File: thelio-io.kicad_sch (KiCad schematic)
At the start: 23 parts, among them Y1 16MHz

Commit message: Layout improvements
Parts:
- USB1: footprint Connector_PinHeader_2.54mm:PinHeader_1x04_P2.54mm_Vertical -> USB:USB_IDC
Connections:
- net GND: now also USB1.7 (GND); no longer USB1.4 (GND)
- net at R1.1: now also USB1.5 (D+); no longer USB1.3 (D+)
- net at USB1.2 (VBUS): no longer R2.1
- new net: R2.1, USB1.3 (D-)
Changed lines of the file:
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@@
       (effects (font (size 1.27 1.27)) hide)
     )
-    (property "Datasheet" "http://www.ti.com/lit/ds/symlink/sn74lvc2g157.pdf" (id 3) (at 200.66 33.02 0)
+    (property "Datasheet" "http://www.ti.com/lit/sg/scyt129e/scyt129e.pdf" (id 3) (at 200.66 33.02 0)
       (effects (font (size 1.27 1.27)) hide)
     )
@@
       (effects (font (size 1.27 1.27)) hide)
     )
-    (property "Datasheet" "" (id 3) (at 183.515 113.03 0)
+    (property "Datasheet" "~" (id 3) (at 183.515 113.03 0)
       (effects (font (size 1.27 1.27)) hide)
     )
@@
       (effects (font (size 1.27 1.27)) hide)
     )
-    (property "Datasheet" "" (id 3) (at 229.235 113.03 0)
+    (property "Datasheet" "~" (id 3) (at 229.235 113.03 0)
       (effects (font (size 1.27 1.27)) hide)
     )
@@
       (effects (font (size 1.27 1.27)) hide)
     )
-    (property "Datasheet" "http://www.ti.com/lit/ds/symlink/sn74lvc2g157.pdf" (id 3) (at 229.87 33.02 0)
+    (property "Datasheet" "http://www.ti.com/lit/sg/scyt129e/scyt129e.pdf" (id 3) (at 229.87 33.02 0)
       (effects (font (size 1.27 1.27)) hide)
     )
@@
   (symbol (lib_id "USB:USB_IDC") (at 111.76 73.66 270) (mirror x) (unit 1)
     (in_bom yes) (on_board yes)
-    (property "Reference" "USB1" (id 0) (at 119.0752 72.6186 90)
-      (effects (font (size 1.27 1.27)) (justify left))
-    )
-    (property "Value" "USB_IDC" (id 1) (at 119.0752 74.93 90)
-      (effects (font (size 1.27 1.27)) (justify left))
-    )
-    (property "Footprint" "Connector_PinHeader_2.54mm:PinHeader_1x04_P2.54mm_Vertical" (id 2) (at 111.76 73.66 0)
+    (property "Reference" "USB1" (id 0) (at 110.49 56.515 90)
+      (effects (font (size 1.27 1.27)) (justify left))
+    )
+    (property "Value" "USB_IDC" (id 1) (at 110.49 66.3448 90)
+      (effects (font (size 1.27 1.27)) (justify left))
+    )
+    (property "Footprint" "USB:USB_IDC" (id 2) (at 111.76 73.66 0)
       (effects (font (size 1.27 1.27)) hide)
     )
@@
     (pin "3")
     (pin "4")
+    (pin "5")
+    (pin "6")
+    (pin "7")
+    (pin "8")
   )
   (symbol (lib_id "power:+12V") (at 266.065 54.61 270) (unit 1)
@@
       (effects (font (size 1.27 1.27)) hide)
     )
-    (property "Datasheet" "http://www.ti.com/lit/ds/symlink/sn74lvc2g157.pdf" (id 3) (at 172.085 33.02 0)
+    (property "Datasheet" "http://www.ti.com/lit/sg/scyt129e/scyt129e.pdf" (id 3) (at 172.085 33.02 0)
       (effects (font (size 1.27 1.27)) hide)
     )
@@
       (effects (font (size 1.27 1.27)) hide)
     )
-    (property "Datasheet" "" (id 3) (at 210.82 86.36 0)
+    (property "Datasheet" "~" (id 3) (at 210.82 86.36 0)
       (effects (font (size 1.27 1.27)) hide)
     )
@@
       (effects (font (size 1.27 1.27)) hide)
     )
-    (property "Datasheet" "http://www.ti.com/lit/ds/symlink/sn74lvc2g157.pdf" (id 3) (at 258.445 33.02 0)
+    (property "Datasheet" "http://www.ti.com/lit/sg/scyt129e/scyt129e.pdf" (id 3) (at 258.445 33.02 0)
       (effects (font (size 1.27 1.27)) hide)
     )
@@
     )
     (path "/24da91e1-4b2d-4e79-a096-b2424715c2dc"
-      (reference "USB1") (unit 1) (value "USB_IDC") (footprint "Connector_PinHeader_2.54mm:PinHeader_1x04_P2.54mm_Vertical")
+      (reference "USB1") (unit 1) (value "USB_IDC") (footprint "USB:USB_IDC")
     )
     (path "/ee06c0cd-13b9-4549-a21e-0082e6f6e36d"

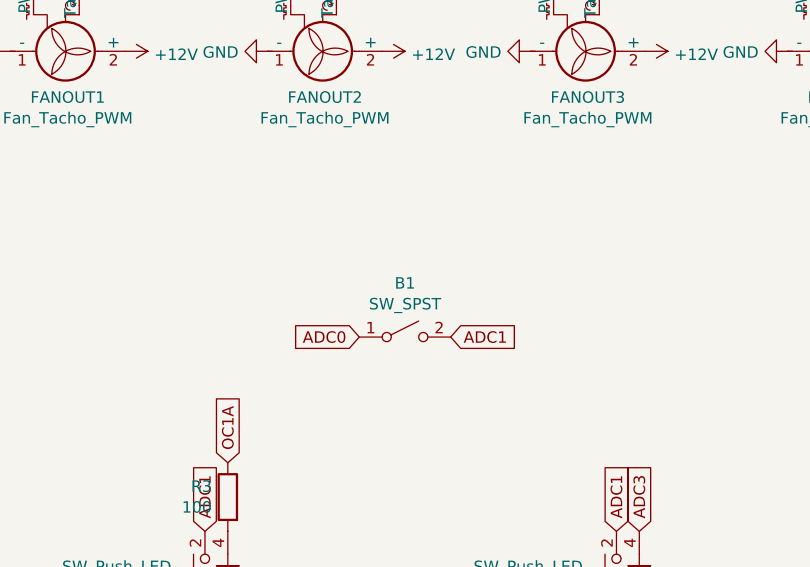
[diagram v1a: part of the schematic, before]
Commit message: Add logo and fix keepouts
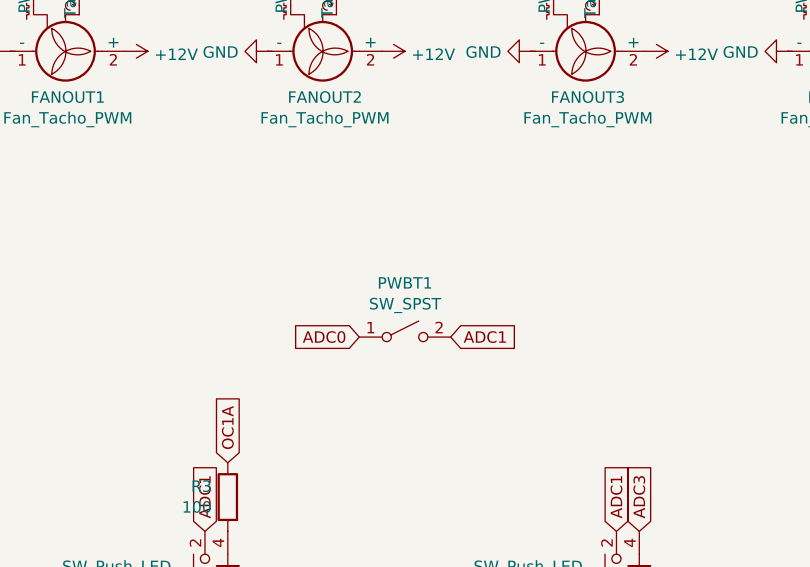
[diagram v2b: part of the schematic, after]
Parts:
- renumbered B1 to PWBT1
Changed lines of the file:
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@@
   (symbol (lib_id "Switch:SW_SPST") (at 210.82 86.36 0) (unit 1)
     (in_bom yes) (on_board yes)
-    (property "Reference" "B1" (id 0) (at 210.82 80.391 0))
+    (property "Reference" "PWBT1" (id 0) (at 210.82 80.391 0))
     (property "Value" "SW_SPST" (id 1) (at 210.82 82.7024 0))
     (property "Footprint" "Button_Switch_SMD:SW_SPST_TL3342" (id 2) (at 210.82 86.36 0)
@@
       (reference "AVR1") (unit 1) (value "ATmega32U4-AU") (footprint "Package_DFN_QFN:QFN-64-1EP_9x9mm_P0.5mm_EP7.5x7.5mm")
     )
-    (path "/7e939f07-8642-4689-8727-9660b52fff9f"
-      (reference "B1") (unit 1) (value "SW_SPST") (footprint "Button_Switch_SMD:SW_SPST_TL3342")
-    )
     (path "/95d7b4e4-d090-4b4b-95d7-0687255342ed"
       (reference "C1") (unit 1) (value "22pF") (footprint "Capacitor_SMD:C_0402_1005Metric")
@@
       (reference "POWER1") (unit 1) (value "ATA_FLOPPY_POWER_4") (footprint "SATA:ATA_FLOPPY_POWER_4")
     )
+    (path "/7e939f07-8642-4689-8727-9660b52fff9f"
+      (reference "PWBT1") (unit 1) (value "SW_SPST") (footprint "Button_Switch_SMD:SW_SPST_TL3342")
+    )
     (path "/0a7c8d68-eedc-46bd-8a41-9ec0add1f19c"

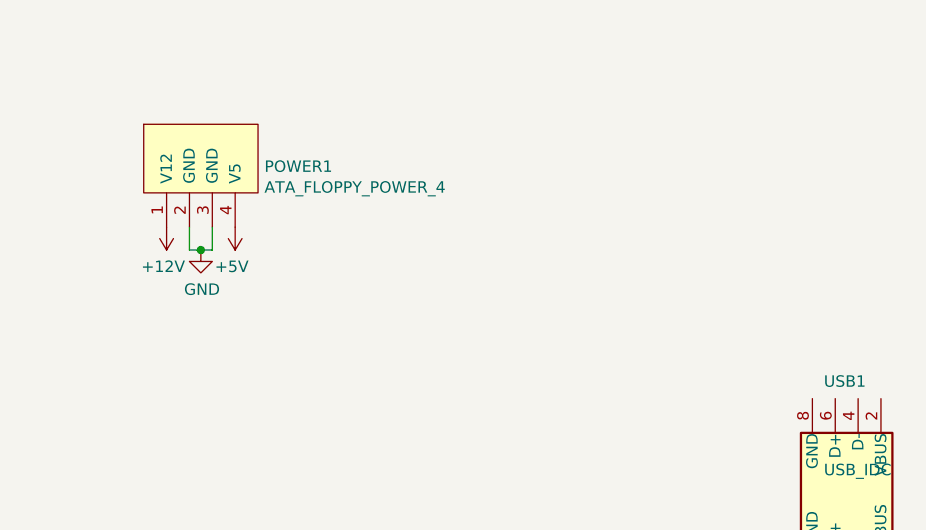
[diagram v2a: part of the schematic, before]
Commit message: Make 4-layer and improve fills
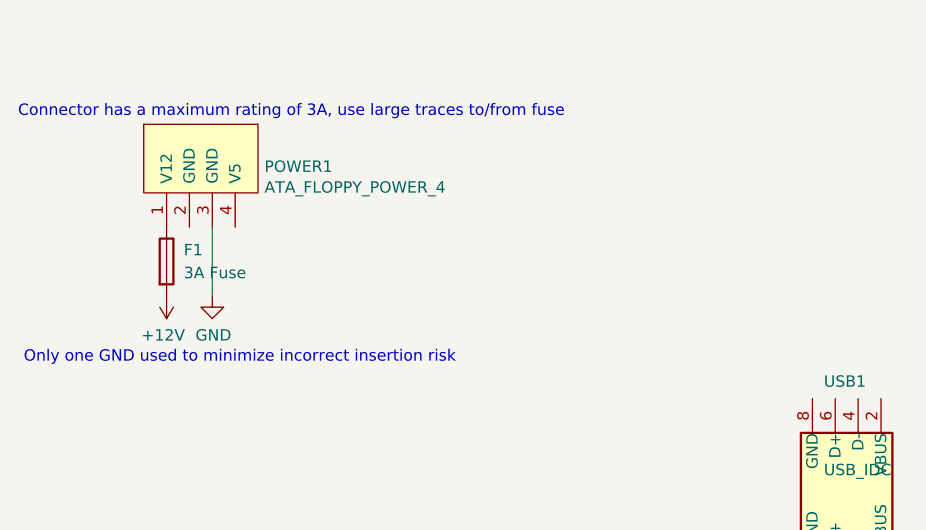
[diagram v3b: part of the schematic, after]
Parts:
- added F1: 3A Fuse, Fuse:Fuse_0603_1608Metric, symbol Device:Fuse
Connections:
- net +12V: now also F1.2; no longer POWER1.1 (V12)
- net GND: no longer POWER1.2 (GND)
- net +5V: no longer names the net of POWER1.4 (V5)
- new net: F1.1, POWER1.1 (V12)
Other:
- note added: "Connector has a maximum rating of 3A, use large traces to/from fuse"
- note added: "Only one GND used to minimize incorrect insertion risk"
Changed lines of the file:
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@@
 (kicad_sch (version 20211123) (generator eeschema)
   (paper "A4")
-  (junction (at 41.275 41.91) (diameter 0) (color 0 0 0 0)
-  )
   (junction (at 133.35 96.52) (diameter 0) (color 0 0 0 0)
   )
@@
   (junction (at 125.73 96.52) (diameter 0) (color 0 0 0 0)
   )
-  (wire (pts (xy 40.005 41.91) (xy 41.275 41.91))
-    (stroke (width 0) (type default) (color 0 0 0 0))
-  )
   (wire (pts (xy 104.14 104.14) (xy 104.14 101.6))
     (stroke (width 0) (type default) (color 0 0 0 0))
@@
     (stroke (width 0) (type default) (color 0 0 0 0))
   )
+  (wire (pts (xy 42.545 39.37) (xy 42.545 46.99))
+    (stroke (width 0) (type default) (color 0 0 0 0))
+  )
   (wire (pts (xy 111.76 92.71) (xy 111.76 104.14))
     (stroke (width 0) (type default) (color 0 0 0 0))
   )
-  (wire (pts (xy 42.545 39.37) (xy 42.545 41.91))
-    (stroke (width 0) (type default) (color 0 0 0 0))
-  )
-  (wire (pts (xy 40.005 39.37) (xy 40.005 41.91))
-    (stroke (width 0) (type default) (color 0 0 0 0))
-  )
   (wire (pts (xy 147.32 119.38) (xy 147.32 121.92))
     (stroke (width 0) (type default) (color 0 0 0 0))
@@
     (stroke (width 0) (type default) (color 0 0 0 0))
   )
-  (wire (pts (xy 42.545 41.91) (xy 41.275 41.91))
-    (stroke (width 0) (type default) (color 0 0 0 0))
-  )
   (wire (pts (xy 109.22 101.6) (xy 109.22 104.14))
     (stroke (width 0) (type default) (color 0 0 0 0))
@@
   (wire (pts (xy 127 104.14) (xy 127 101.6))
     (stroke (width 0) (type default) (color 0 0 0 0))
+  )
+  (text "Only one GND used to minimize incorrect insertion risk"
+    (at 21.59 54.61 0)
+    (effects (font (size 1.27 1.27)) (justify left bottom))
   )
   (text "Add diode on VCC" (at 124.46 82.55 0)
     (effects (font (size 1.27 1.27)) (justify left bottom))
   )
+  (text "Connector has a maximum rating of 3A, use large traces to/from fuse"
+    (at 20.955 27.305 0)
+    (effects (font (size 1.27 1.27)) (justify left bottom))
+  )
   (text "Use chip protection and filter on VBUS" (at 116.84 80.01 0)
     (effects (font (size 1.27 1.27)) (justify left bottom))
@@
     (pin "4")
   )
-  (symbol (lib_id "power:+5V") (at 45.085 39.37 180) (unit 1)
-    (in_bom yes) (on_board yes)
-    (property "Reference" "#PWR07" (id 0) (at 45.085 35.56 0)
-      (effects (font (size 1.27 1.27)) hide)
-    )
-    (property "Value" "+5V" (id 1) (at 44.704 43.7642 0))
-    (property "Footprint" "" (id 2) (at 45.085 39.37 0)
-      (effects (font (size 1.27 1.27)) hide)
-    )
-    (property "Datasheet" "" (id 3) (at 45.085 39.37 0)
-      (effects (font (size 1.27 1.27)) hide)
-    )
-    (pin "1")
-  )
-  (symbol (lib_id "power:GND") (at 41.275 41.91 0) (unit 1)
-    (in_bom yes) (on_board yes)
-    (property "Reference" "#PWR05" (id 0) (at 41.275 48.26 0)
-      (effects (font (size 1.27 1.27)) hide)
-    )
-    (property "Value" "GND" (id 1) (at 41.402 46.3042 0))
-    (property "Footprint" "" (id 2) (at 41.275 41.91 0)
-      (effects (font (size 1.27 1.27)) hide)
-    )
-    (property "Datasheet" "" (id 3) (at 41.275 41.91 0)
-      (effects (font (size 1.27 1.27)) hide)
-    )
-    (pin "1")
-  )
-  (symbol (lib_id "power:+12V") (at 37.465 39.37 180) (unit 1)
-    (in_bom yes) (on_board yes)
-    (property "Reference" "#PWR04" (id 0) (at 37.465 35.56 0)
-      (effects (font (size 1.27 1.27)) hide)
-    )
-    (property "Value" "+12V" (id 1) (at 37.084 43.7642 0))
-    (property "Footprint" "" (id 2) (at 37.465 39.37 0)
-      (effects (font (size 1.27 1.27)) hide)
-    )
-    (property "Datasheet" "" (id 3) (at 37.465 39.37 0)
+  (symbol (lib_id "power:GND") (at 42.545 46.99 0) (unit 1)
+    (in_bom yes) (on_board yes)
+    (property "Reference" "#PWR05" (id 0) (at 42.545 53.34 0)
+      (effects (font (size 1.27 1.27)) hide)
+    )
+    (property "Value" "GND" (id 1) (at 42.672 51.3842 0))
+    (property "Footprint" "" (id 2) (at 42.545 46.99 0)
+      (effects (font (size 1.27 1.27)) hide)
+    )
+    (property "Datasheet" "" (id 3) (at 42.545 46.99 0)
+      (effects (font (size 1.27 1.27)) hide)
+    )
+    (pin "1")
+  )
+  (symbol (lib_id "power:+12V") (at 37.465 46.99 180) (unit 1)
+    (in_bom yes) (on_board yes)
+    (property "Reference" "#PWR04" (id 0) (at 37.465 43.18 0)
+      (effects (font (size 1.27 1.27)) hide)
+    )
+    (property "Value" "+12V" (id 1) (at 37.084 51.3842 0))
+    (property "Footprint" "" (id 2) (at 37.465 46.99 0)
+      (effects (font (size 1.27 1.27)) hide)
+    )
+    (property "Datasheet" "" (id 3) (at 37.465 46.99 0)
       (effects (font (size 1.27 1.27)) hide)
     )
@@
     (pin "8")
   )
+  (symbol (lib_id "Device:Fuse") (at 37.465 43.18 0) (unit 1)
+    (in_bom yes) (on_board yes) (fields_autoplaced)
+    (property "Reference" "F1" (id 0) (at 39.37 41.9099 0)
+      (effects (font (size 1.27 1.27)) (justify left))
+    )
+    (property "Value" "3A Fuse" (id 1) (at 39.37 44.4499 0)
+      (effects (font (size 1.27 1.27)) (justify left))
+    )
+    (property "Footprint" "Fuse:Fuse_0603_1608Metric" (id 2) (at 35.687 43.18 90)
+      (effects (font (size 1.27 1.27)) hide)
+    )
+    (property "Datasheet" "~" (id 3) (at 37.465 43.18 0)
+      (effects (font (size 1.27 1.27)) hide)
+    )
+    (pin "1")
+    (pin "2")
+  )
   (symbol (lib_id "power:GND") (at 253.365 54.61 270) (unit 1)
     (in_bom yes) (on_board yes)
@@
       (reference "#PWR06") (unit 1) (value "GND") (footprint "")
     )
-    (path "/00000000-0000-0000-0000-00005b9b7b20"
-      (reference "#PWR07") (unit 1) (value "+5V") (footprint "")
-    )
     (path "/4ebcb7f1-37d9-4c1e-aaa5-5ab3fcdffadd"
       (reference "#PWR08") (unit 1) (value "VCC") (footprint "")
@@
       (reference "C3") (unit 1) (value "22pF") (footprint "Capacitor_SMD:C_0402_1005Metric")
     )
+    (path "/684a5de3-a519-44ea-bebe-5a3b8e01f198"
+      (reference "F1") (unit 1) (value "3A Fuse") (footprint "Fuse:Fuse_0603_1608Metric")
+    )
     (path "/58aa2d3c-9f87-445b-8b99-8ae14894c0ec"
